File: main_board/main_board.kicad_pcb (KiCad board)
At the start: 2 copper layers, 160 x 110 mm, 147 parts, among them IC1 MP2722GRH-0000-Z, IC2 MP3429GL-Z, IC3 NX3DV42GU, IC4 TS921ID, IC5 CY7C65632-28LTXC, IC6 TS921ID, J1 USB3_A, J10 Conn_01x22_Female, J2 USB3_A, J22 690-019-298-412, J3 Bus_M.2_Socket_M, J4 USB_B_Micro, J5 USB_C_Receptacle_USB2.0, J6 USB_A, J7 USB_A, J8 AudioJack3, U1 AP3441SHE-7B, U12 RT9742SNGV, U2 ASEK-32.768KHZ-L-R-T, U3 ATmega32U4-M, U4 AP22653W6, U5 AP2204RB-3.3, U6 AP22653W6, Y1 Crystal, Y2 Crystal

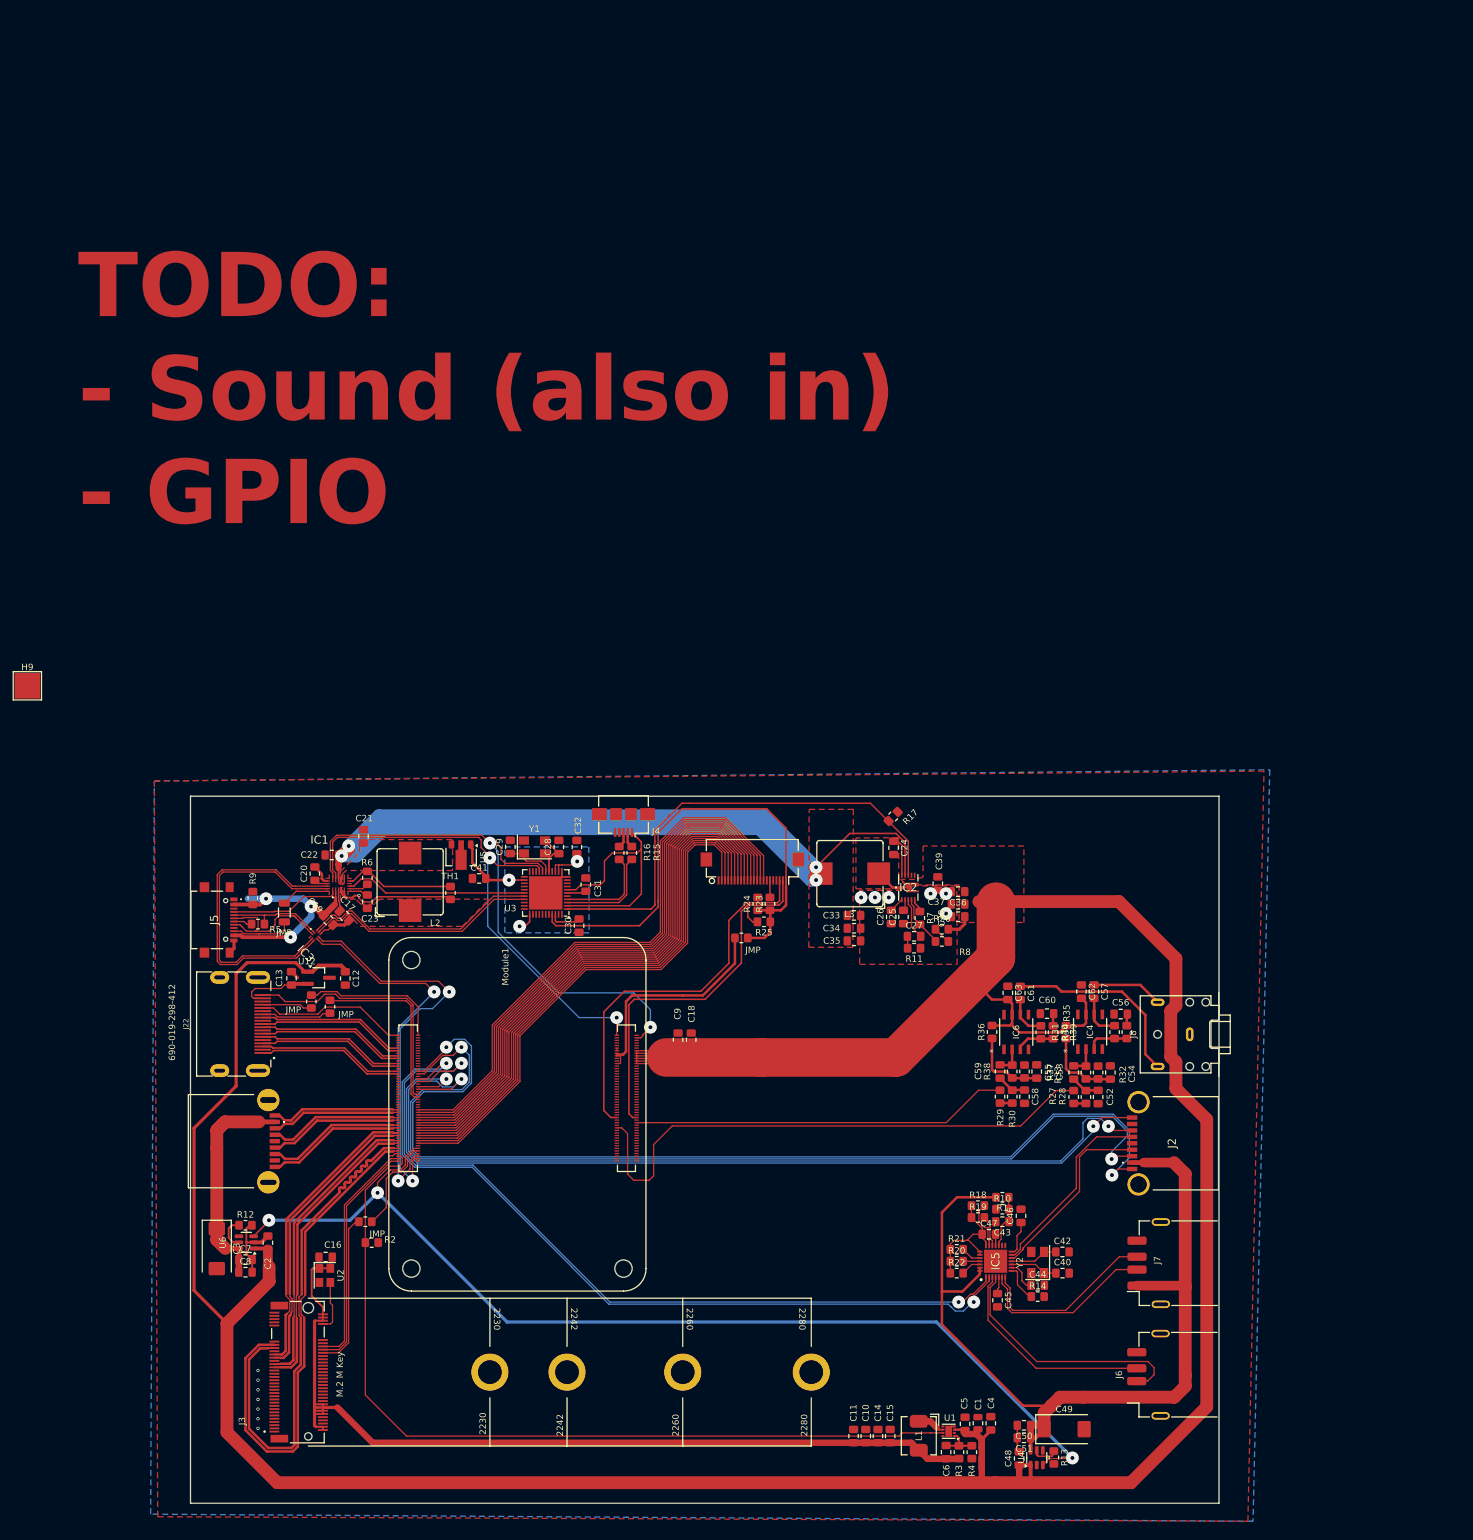
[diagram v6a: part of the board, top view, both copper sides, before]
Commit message: Implement power monitoring
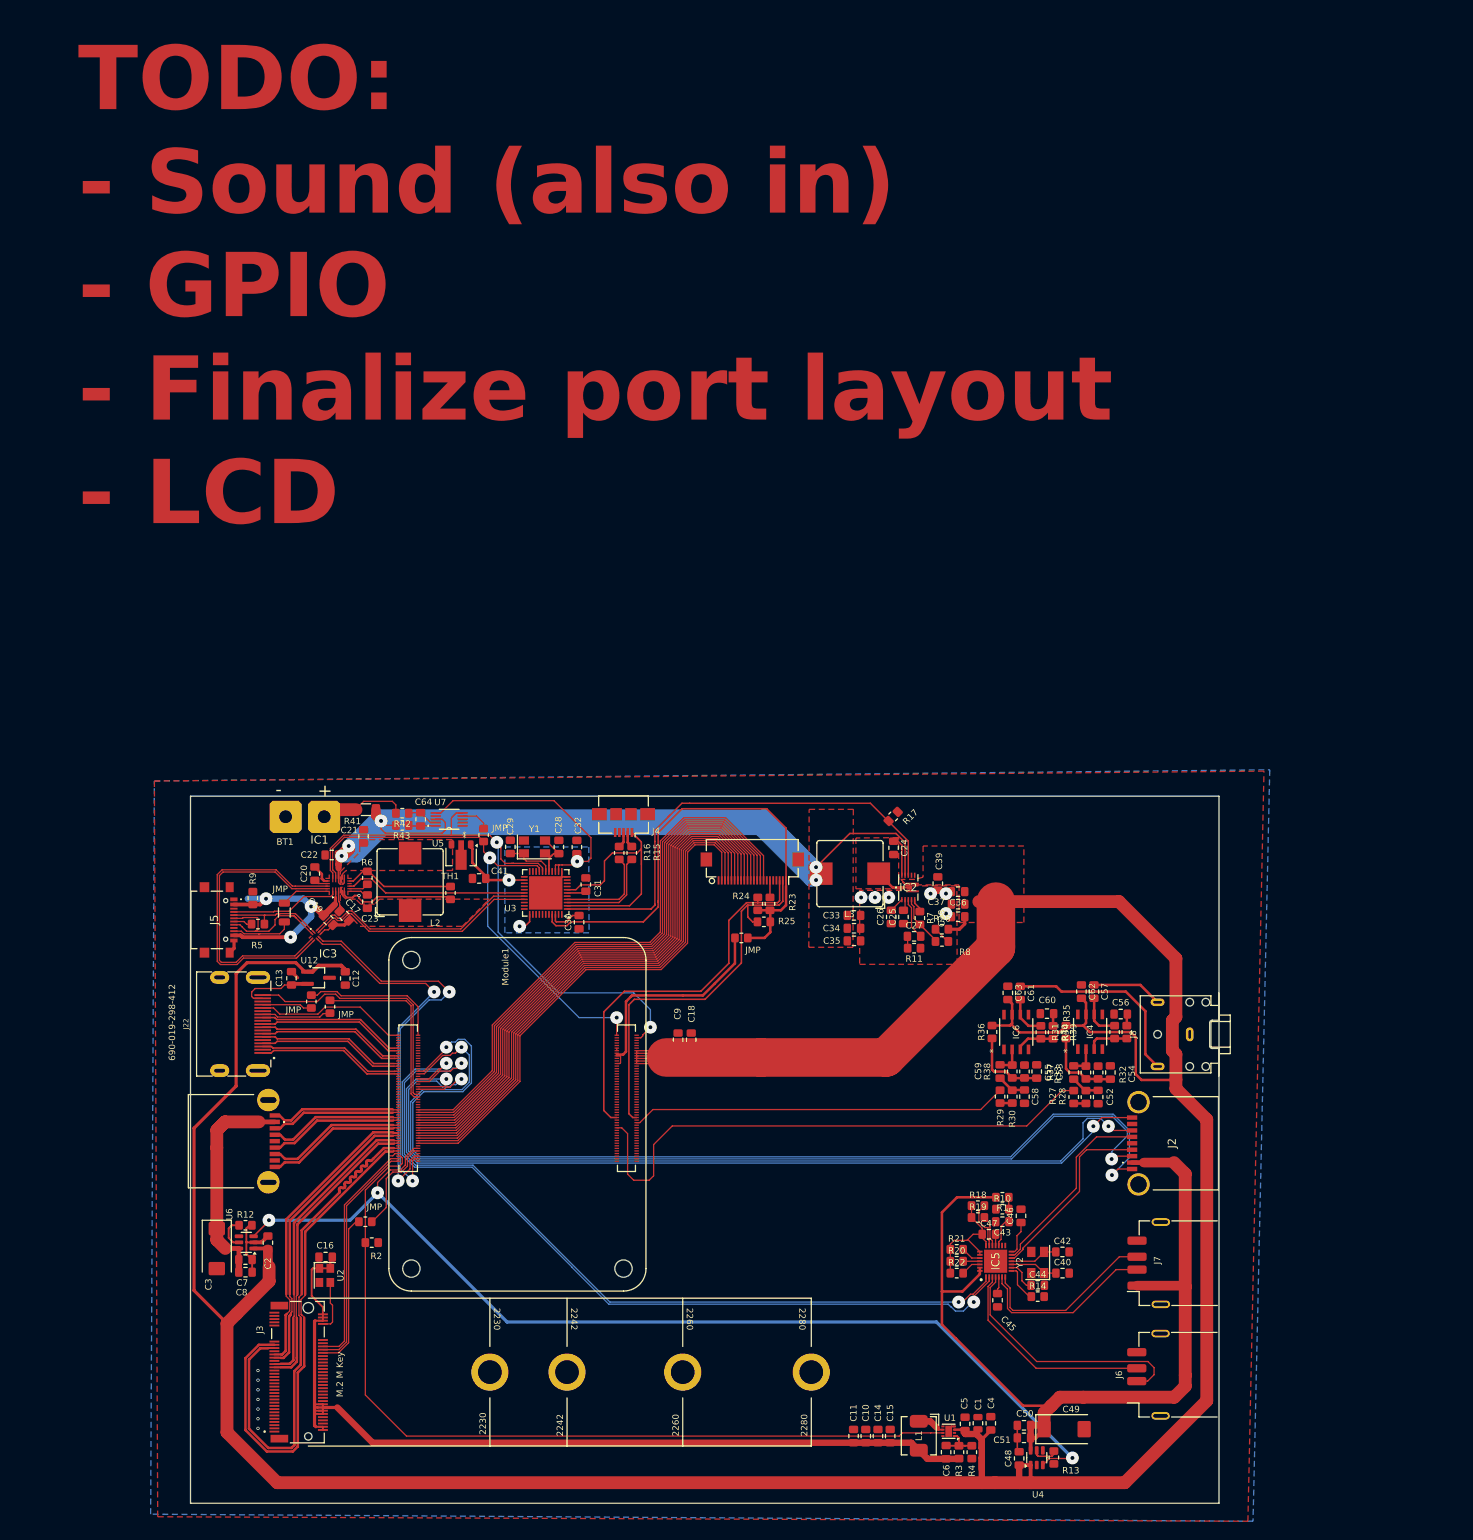
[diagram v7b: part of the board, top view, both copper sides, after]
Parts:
- removed H9: BAT_PAD, TestPoint:TestPoint_Pad_4.0x4.0mm
- added BT1: Battery_Cell, 000_custom:Bat_terminal, F.Cu at (48.7, 22.9)
- added C64: 100n, Capacitor_SMD:C_0805_2012Metric_Pad1.18x1.45mm_HandSolder, F.Cu at (63.7, 23.3)
- added JMP: R_0805_2012Metric_Pad1.20x1.40mm_HandSolder, Resistor_SMD:R_0805_2012Metric_Pad1.20x1.40mm_HandSolder, F.Cu at (73.5, 25.8)
- added R41: 0.01R, Resistor_SMD:R_1206_3216Metric_Pad1.30x1.75mm_HandSolder, F.Cu at (55.2, 21.8)
- added R42: 10R, Resistor_SMD:R_0805_2012Metric_Pad1.20x1.40mm_HandSolder, F.Cu at (60.9, 22.4)
- added R43: 10R, Resistor_SMD:R_0805_2012Metric_Pad1.20x1.40mm_HandSolder, F.Cu at (60.9, 24.2)
- added U7: INA220AIDGST, 000_custom:DGS10, F.Cu at (68.1, 23.3)
- moved C30 0.54 mm to (88.3, 39.3)
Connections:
- net /CM5_GPIO/GPIO25 renamed /CM5_GPIO/AUDIO_IN_CLK
- net /CM5_GPIO/GPIO26 renamed /CM5_GPIO/AUDIO_IN_DATA
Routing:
- net /Battery management/PMIC_3.3V: track 21.0 -> 53.9 mm
- net /Battery management/VBAT: track 187.3 -> 206.6 mm, vias 4 -> 5
- net Net-(BT1-+): track 0.00 -> 13.5 mm
- net /Battery management/+5V: track 523.1 -> 536.1 mm
- net Net-(U7-VIN-): track 0.00 -> 4.87 mm
- net Net-(U7-VIN+): track 0.00 -> 4.25 mm
- net /Battery management/IIC_SDA: track 81.8 -> 85.8 mm
- net /Battery management/IIC_SCL: track 92.1 -> 96.0 mm
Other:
- board text added: "TODO: - Sound (also in) - GPIO - Finalize port layout - LCD"
- board text removed: "TODO: - Sound (also in) - GPIO"

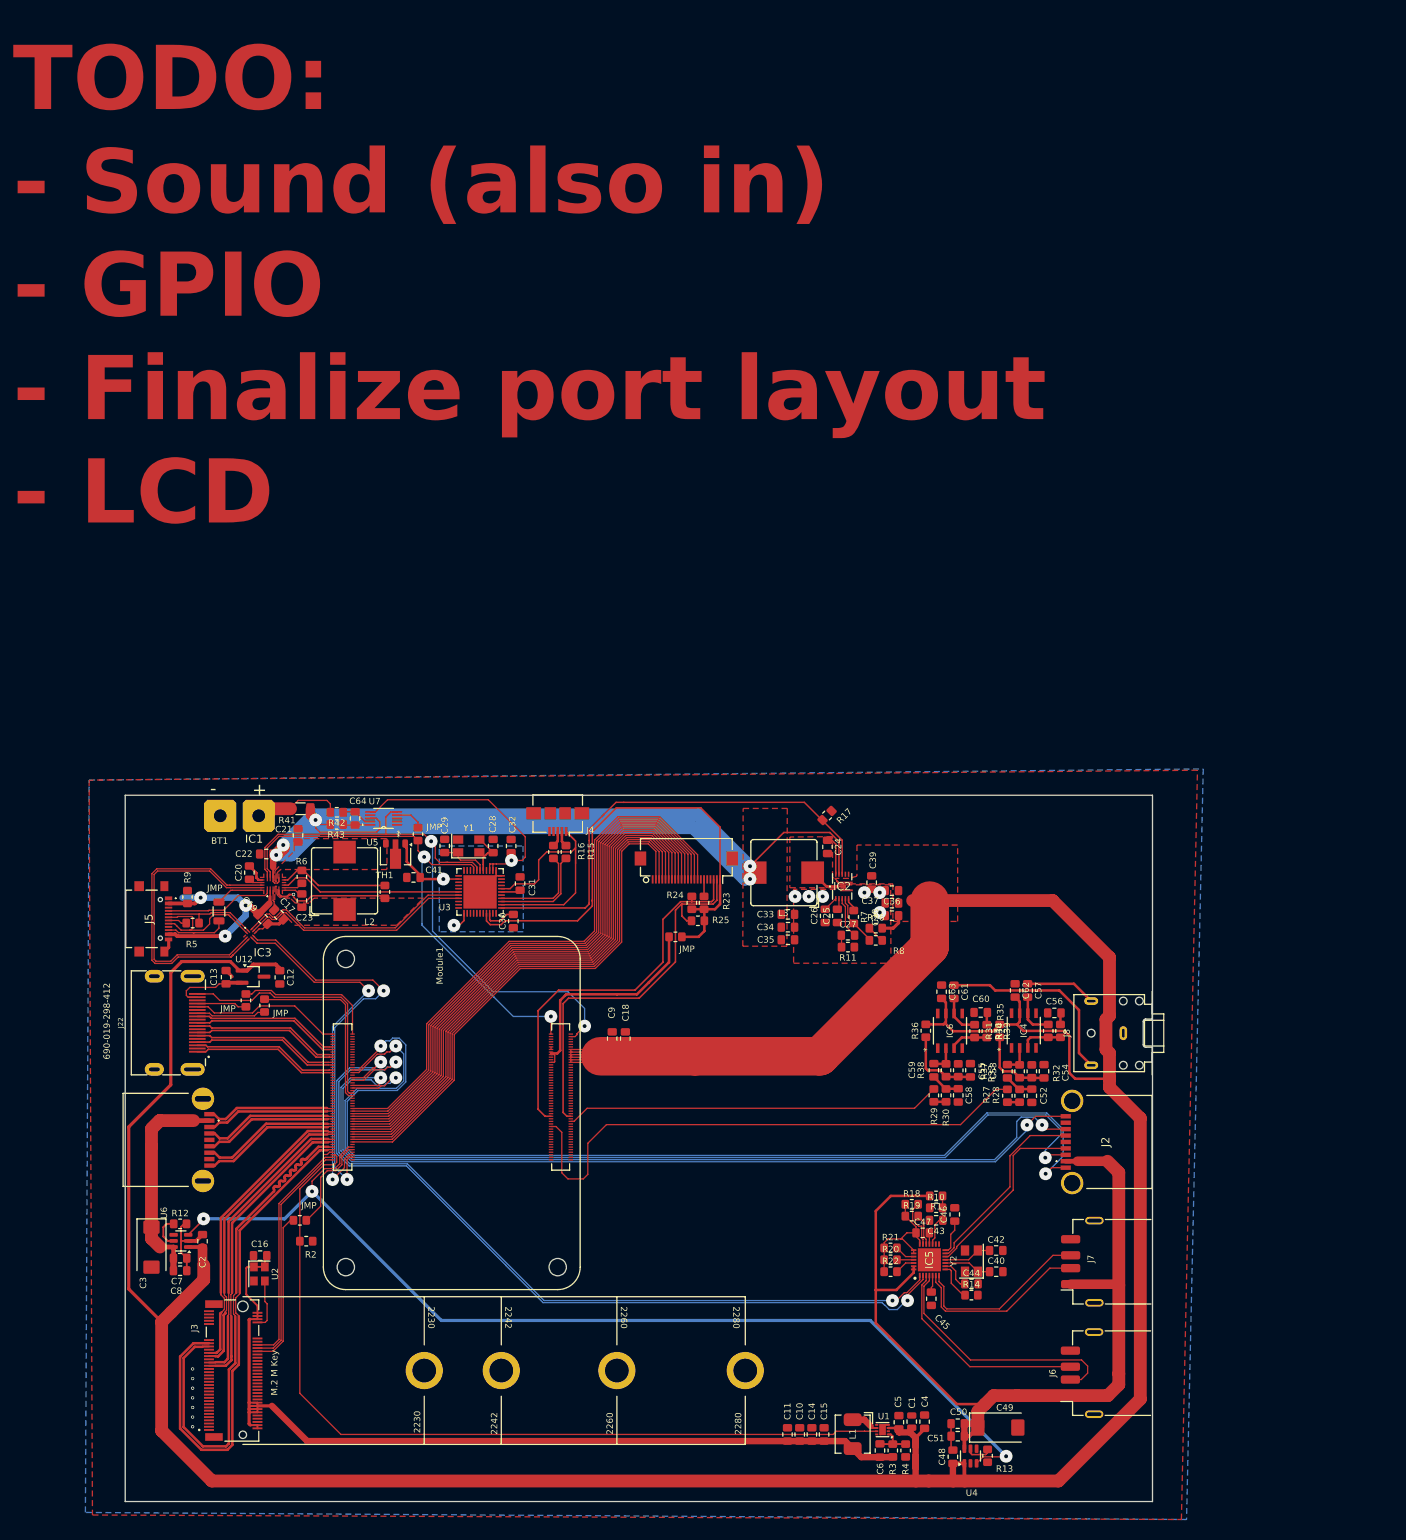
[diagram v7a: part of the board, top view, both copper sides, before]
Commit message: Add expansion slot
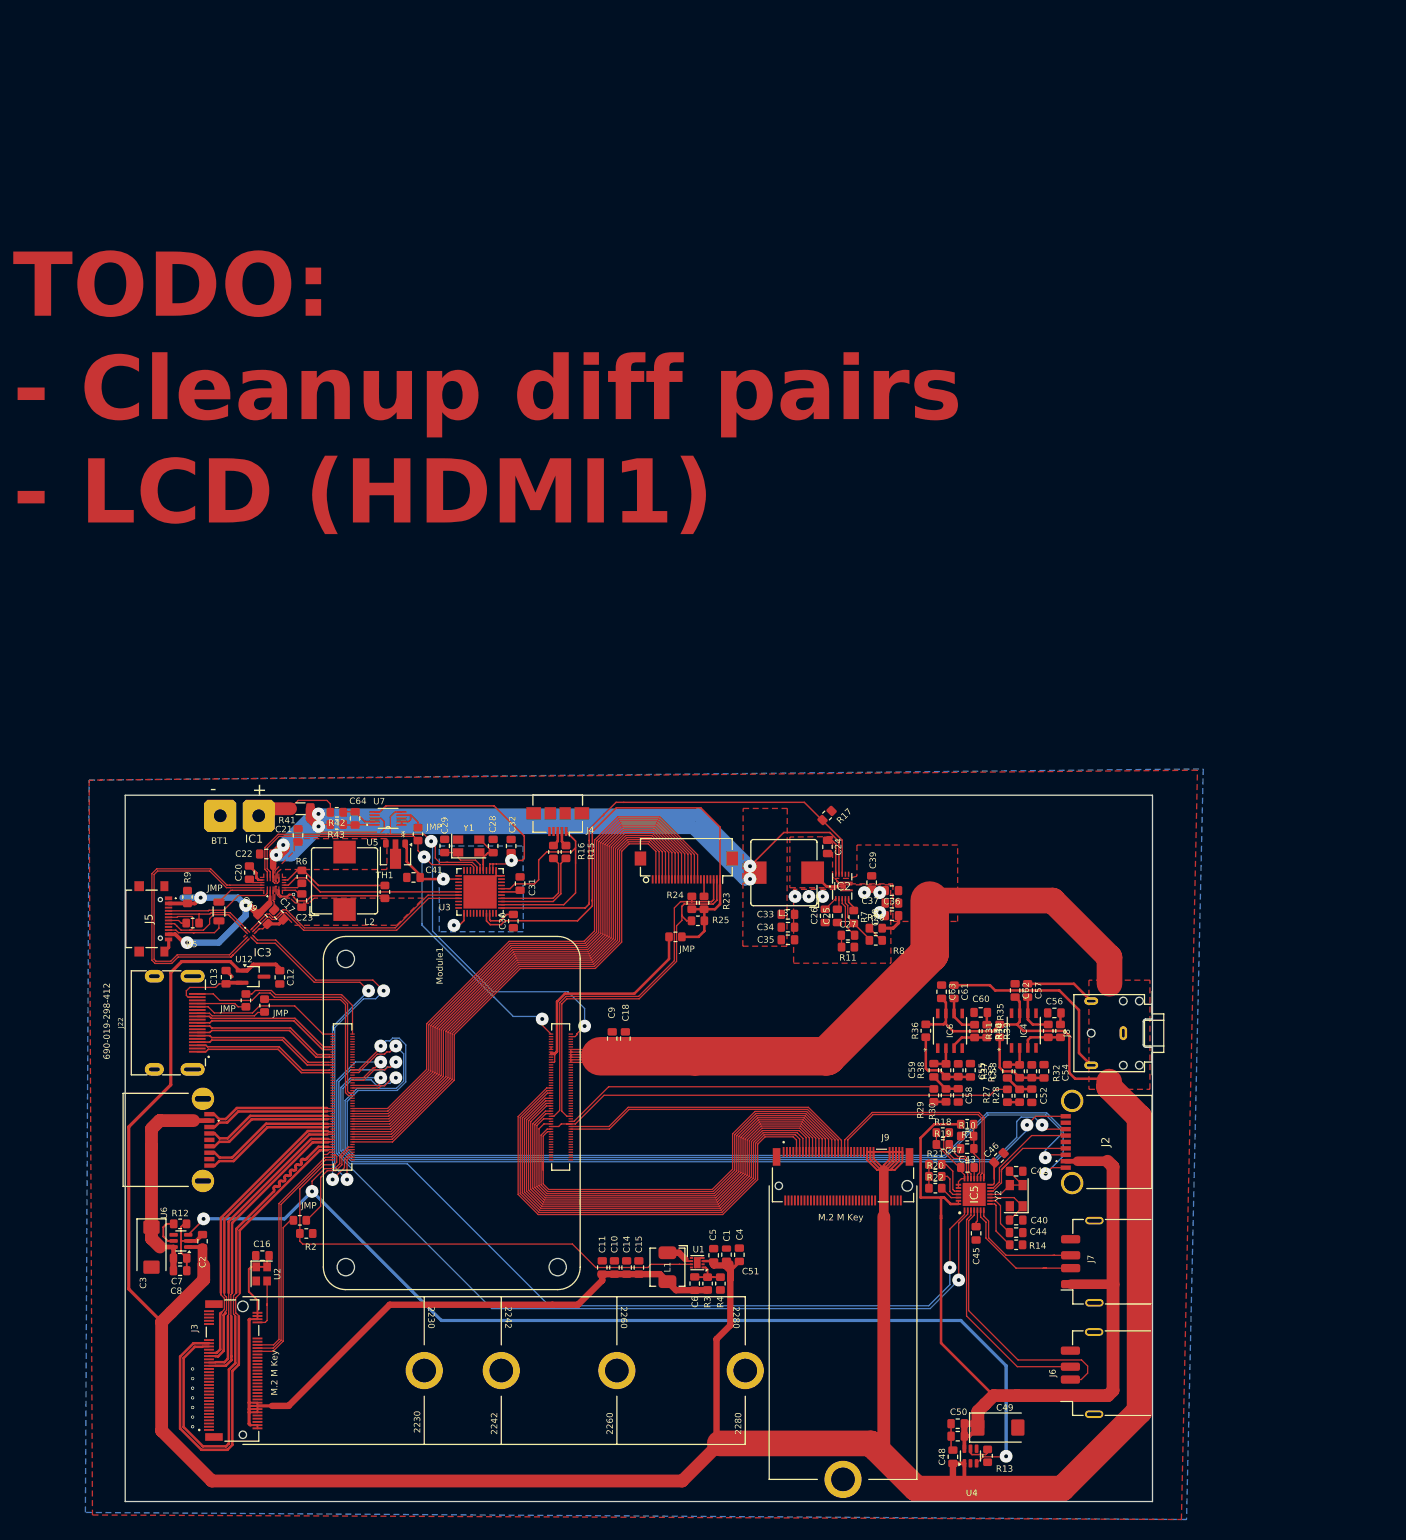
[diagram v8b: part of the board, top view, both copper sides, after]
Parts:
- added J9: The_card, 000_custom:Random card conn, F.Cu at (139.7, 80.5)
- moved C1 38.8 mm to (121.5, 91.2)
- moved C11 38.8 mm to (102.2, 93.2)
- moved C14 38.8 mm to (106.0, 93.2)
- moved C4 38.8 mm to (123.5, 91.3)
- moved C5 38.8 mm to (119.5, 91.3)
- moved C10 38.8 mm to (104.1, 93.2)
- moved C15 38.8 mm to (107.9, 93.2)
- moved L1 38.8 mm to (112.3, 93.2)
- moved R3 38.8 mm to (118.6, 95.8)
- moved R4 38.8 mm to (120.6, 95.8)
- moved U1 38.8 mm to (117.0, 92.5)
- moved C6 38.8 mm to (116.6, 95.8)
- moved R20 14.8 mm to (154.1, 79.0)
- moved R21 14.8 mm to (154.1, 77.2)
- moved R22 14.8 mm to (154.1, 80.9)
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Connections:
- IC1 pad 20: /Battery management/USBC_MX2_USB2_P -> /Battery management/USBC_MX2_USB2_N
- IC1 pad 21: /Battery management/USBC_MX2_USB2_N -> /Battery management/USBC_MX2_USB2_P
- IC3 pad 4: /Battery management/USBC_MX2_USB2_N -> /Battery management/USBC_MX2_USB2_P
- IC3 pad 5: /Battery management/USBC_MX2_USB2_P -> /Battery management/USBC_MX2_USB2_N
- IC5 pad 15: /USB hub/USB2_2_DN -> /The card/USB2_2_DN
- IC5 pad 16: /USB hub/USB2_2_DP -> /The card/USB2_2_DP
- Module1 pad 24: /CM5_GPIO/AUDIO_IN_DATA -> /CM5_GPIO/GP26
- Module1 pad 25: /CM5_GPIO/GPIO21 -> /CM5_GPIO/GP21
- Module1 pad 26: /CM5_GPIO/GPIO19 -> /CM5_GPIO/GP19
- Module1 pad 27: /CM5_GPIO/GPIO20 -> /CM5_GPIO/GP20
- Module1 pad 29: /CM5_GPIO/GPIO16 -> /CM5_GPIO/AUDIO_OUT_L
- Module1 pad 30: /CM5_GPIO/GPIO6 -> /CM5_GPIO/GP6
- Module1 pad 34: /CM5_GPIO/GPIO5 -> /CM5_GPIO/GP5
- Module1 pad 38: /CM5_GPIO/GPIO11 -> /CM5_GPIO/GP11
- Module1 pad 40: /CM5_GPIO/GPIO9 -> /CM5_GPIO/GP9
- Module1 pad 44: /CM5_GPIO/GPIO10 -> /CM5_GPIO/GP10
- Module1 pad 46: /CM5_GPIO/GPIO22 -> /CM5_GPIO/GP22
- Module1 pad 48: /CM5_GPIO/GPIO27 -> /CM5_GPIO/GP27
- Module1 pad 50: /CM5_GPIO/GPIO17 -> /CM5_GPIO/GP17
- Module1 pad 54: /CM5_GPIO/GPIO4 -> /CM5_GPIO/GP4
- Module1 pad 56: /CM5_GPIO/GPIO3 -> /CM5_GPIO/GP3
- Module1 pad 58: /CM5_GPIO/GPIO2 -> /CM5_GPIO/GP2
- U7 pad 1: GND -> /Battery management/IIC_SDA
- U7 pad 2: GND -> /Battery management/IIC_SDA
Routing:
- net /Battery management/+5V: track 536.1 -> 637.5 mm
- net /CM5_GPIO/GP2: track 0.00 -> 74.0 mm
- net /CM5_GPIO/GP3: track 0.00 -> 73.6 mm
- net /CM5_GPIO/GP4: track 0.00 -> 73.2 mm
- net /CM5_GPIO/GP17: track 0.00 -> 72.7 mm
- net /CM5_GPIO/GP27: track 0.00 -> 72.2 mm
- net /CM5_GPIO/GP22: track 0.00 -> 71.7 mm
- net /CM5_GPIO/GP10: track 0.00 -> 71.2 mm
- net /CM5_GPIO/GP9: track 0.00 -> 70.5 mm
- net /CM5_GPIO/GP11: track 0.00 -> 70.0 mm
- net /CM5_GPIO/GP5: track 0.00 -> 69.3 mm
- net /CM5_GPIO/GP6: track 0.00 -> 68.4 mm
- net /CM5_GPIO/GP26: track 0.00 -> 68.0 mm
- net /CM5_GPIO/GP19: track 0.00 -> 67.3 mm
- net /CM5_HighSpeed/PCIE_PWR_EN: track 133.7 -> 80.2 mm
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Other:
- board text added: "TODO: - Cleanup diff pairs - LCD (HDMI1)"
- board text removed: "TODO: - Sound (also in) - GPIO - Finalize port layout - LCD"
